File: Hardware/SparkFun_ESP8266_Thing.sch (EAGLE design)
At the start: 72 parts, among them J1 DNP, Q1 2.5A/30V, U1 ESP8266, U2 MCP73831, U3 AT25SF041-SOIC8, U4 AP2112K-3.3V, U5 DNP, U6 DNP, U7 DNP, Y1 26MHz

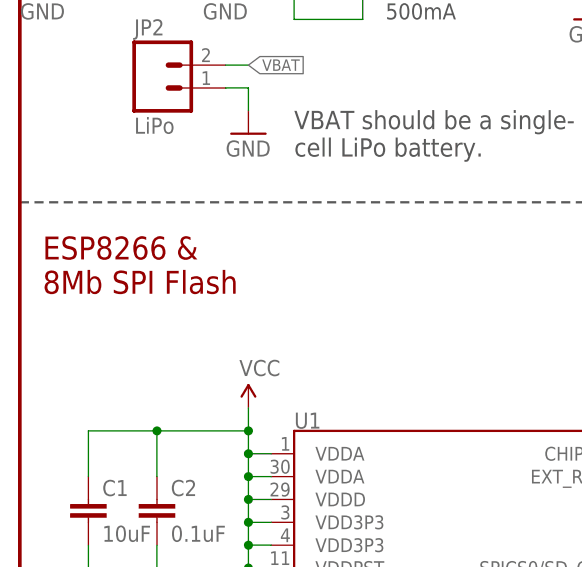
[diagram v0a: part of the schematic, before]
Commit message: Fixing flash size information in schematic.
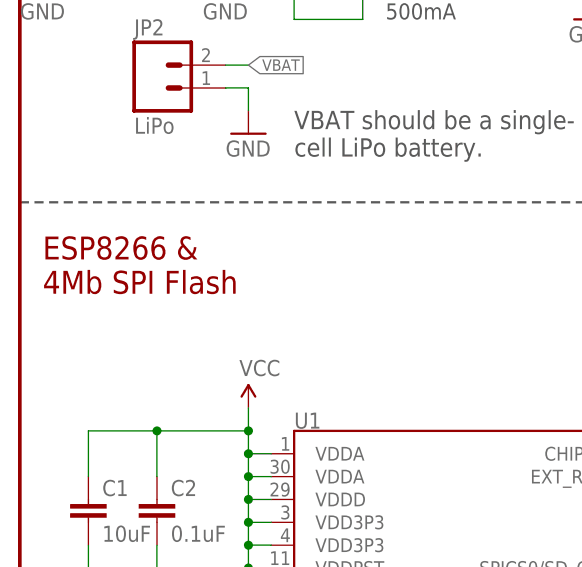
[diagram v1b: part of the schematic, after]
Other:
- note added: "ESP8266 & 4Mb SPI Flash"
- note removed: "ESP8266 & 8Mb SPI Flash"
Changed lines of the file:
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@@
 <layer number="254" name="cooling" color="7" fill="1" visible="yes" active="yes"/>
 </layers>
-<schematic xreflabel="%F%N/%S.%C%R" xrefpart="/%S.%C%R">
+<schematic xreflabel="%F%N/%S" xrefpart="/%S.%C%R">
 <attributes>
 </attributes>
@@
 LiPo Charger</text>
 <text x="2.54" y="116.84" size="2.54" layer="94">ESP8266 &amp;
-8Mb SPI Flash</text>
+4Mb SPI Flash</text>
 <text x="149.86" y="104.14" size="2.54" layer="94">Headers</text>
 <wire x1="147.32" y1="63.5" x2="248.92" y2="63.5" width="0.254" layer="97" style="shortdash"/>

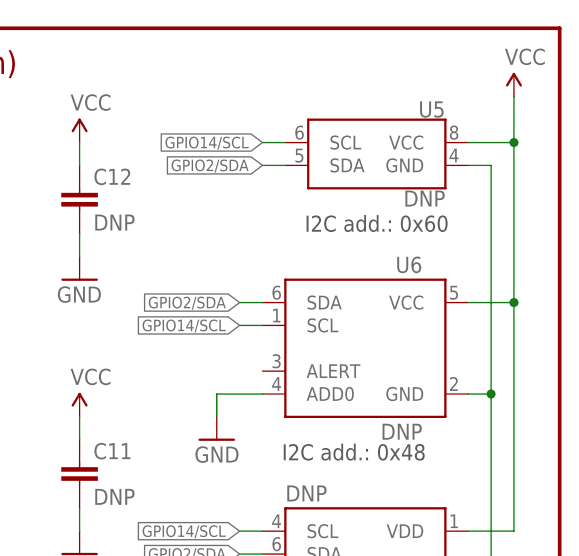
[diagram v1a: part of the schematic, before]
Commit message: Mapping new parts to equivalent devices in the SparkFun libraries.
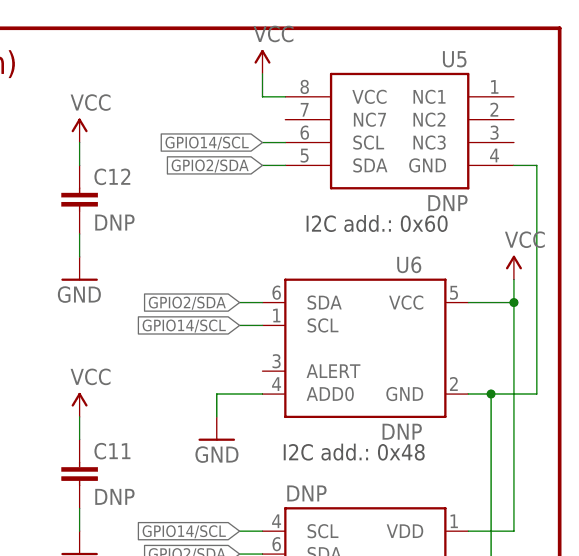
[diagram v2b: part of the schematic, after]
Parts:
- E1: device esp8266-development-board:ANTENNATRACE -> SparkFun-RF:ANTENNATRACE
- U1: device esp8266-development-board:ESP8266 -> SparkFun-RF:ESP8266
- U3: device esp8266-development-board:AT25SF041-SOIC8 -> SparkFun-DigitalIC:AT25SF041-SOIC8
- U5: device esp8266-development-board:ATECC108-MAHDA -> SparkFun-DigitalIC:ATECC108-MAHDA
- U7: device esp8266-development-board:TSL2561FN -> SparkFun-Sensors:TSL2561FN
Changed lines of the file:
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@@
 <layer number="56" name="wert" color="7" fill="1" visible="no" active="no"/>
 <layer number="57" name="tCAD" color="7" fill="1" visible="no" active="no"/>
+<layer number="59" name="tCarbon" color="7" fill="1" visible="no" active="no"/>
+<layer number="60" name="bCarbon" color="7" fill="1" visible="no" active="no"/>
 <layer number="90" name="Modules" color="5" fill="1" visible="yes" active="yes"/>
 <layer number="91" name="Nets" color="2" fill="1" visible="yes" active="yes"/>
@@
 <layer number="113" name="IDFDebug" color="7" fill="1" visible="yes" active="yes"/>
 <layer number="116" name="Patch_BOT" color="9" fill="4" visible="yes" active="yes"/>
+<layer number="118" name="Rect_Pads" color="7" fill="1" visible="yes" active="yes"/>
 <layer number="121" name="_tsilk" color="7" fill="1" visible="yes" active="yes"/>
 <layer number="122" name="_bsilk" color="7" fill="1" visible="yes" active="yes"/>
@@
 <layer number="127" name="_tValues" color="7" fill="1" visible="yes" active="yes"/>
 <layer number="128" name="_bValues" color="7" fill="1" visible="yes" active="yes"/>
+<layer number="129" name="Mask" color="7" fill="1" visible="yes" active="yes"/>
 <layer number="131" name="tAdjust" color="7" fill="1" visible="yes" active="yes"/>
 <layer number="132" name="bAdjust" color="7" fill="1" visible="yes" active="yes"/>
@@
 <layer number="251" name="SMDround" color="12" fill="11" visible="no" active="no"/>
 <layer number="254" name="cooling" color="7" fill="1" visible="yes" active="yes"/>
+<layer number="255" name="routoute" color="7" fill="1" visible="yes" active="yes"/>
 </layers>
 <schematic xreflabel="%F%N/%S" xrefpart="/%S.%C%R">
@@
 <parts>
 <part name="FRAME1" library="SparkFun-Aesthetics" deviceset="FRAME-LETTER" device=""/>
-<part name="U1" library="esp8266-development-board" deviceset="ESP8266" device=""/>
+<part name="U1" library="SparkFun-RF" deviceset="ESP8266" device=""/>
 <part name="SUPPLY1" library="SparkFun-Aesthetics" deviceset="VCC" device=""/>
 <part name="C1" library="SparkFun-Capacitors" deviceset="10UF-6.3V-20%(0603)" device="" value="10uF"/>
@@
 <part name="SUPPLY7" library="SparkFun-Aesthetics" deviceset="VCC" device=""/>
 <part name="GND20" library="SparkFun-Aesthetics" deviceset="GND" device=""/>
-<part name="U3" library="esp8266-development-board" deviceset="AT25SF041" device="-SOIC8"/>
-<part name="U5" library="esp8266-development-board" deviceset="ATECC108" device="-MAHDA" value="DNP"/>
+<part name="U3" library="SparkFun-DigitalIC" deviceset="AT25SF041" device="-SOIC8"/>
+<part name="U5" library="SparkFun-DigitalIC" deviceset="ATECC108" device="-MAHDA" value="DNP"/>
 <part name="SUPPLY13" library="SparkFun-Aesthetics" deviceset="VCC" device=""/>
 <part name="R13" library="SparkFun-Resistors" deviceset="2.2KOHM1/10W1%(0603)" device="" value="2.2k"/>
@@
 <part name="LOGO3" library="SparkFun-Aesthetics" deviceset="SFE_LOGO_FLAME" device=".1_INCH"/>
 <part name="LOGO4" library="SparkFun-Aesthetics" deviceset="OSHW-LOGO" device="S"/>
-<part name="E1" library="esp8266-development-board" deviceset="ANTENNA" device="TRACE" value="ANTENNATRACE"/>
+<part name="E1" library="SparkFun-RF" deviceset="ANTENNA" device="TRACE" value="ANTENNATRACE"/>
 <part name="GND18" library="SparkFun-Aesthetics" deviceset="GND" device=""/>
 <part name="C3" library="SparkFun-Capacitors" deviceset="10PF-50V-5%(0603)" device="" value="10pF"/>
@@
 <part name="SUPPLY12" library="SparkFun-Aesthetics" deviceset="VIN" device=""/>
 <part name="GND24" library="SparkFun-Aesthetics" deviceset="GND" device=""/>
-<part name="U7" library="esp8266-development-board" deviceset="TSL2561" device="FN" value="DNP"/>
+<part name="U7" library="SparkFun-Sensors" deviceset="TSL2561" device="FN" value="DNP"/>
 <part name="GND31" library="SparkFun-Aesthetics" deviceset="GND" device=""/>
 <part name="SUPPLY17" library="SparkFun-Aesthetics" deviceset="VCC" device=""/>
@@
 <part name="SJ1" library="SparkFun-Passives" deviceset="JUMPER-PAD-2-NC_BY_TRACE" device="" value=""/>
 <part name="R4" library="SparkFun-Resistors" deviceset="2.0KOHM1/10W5%(0603)" device="" value="2.0k"/>
+<part name="SUPPLY16" library="SparkFun-Aesthetics" deviceset="VCC" device=""/>
 </parts>
 <sheets>
@@
 <instance part="GND20" gate="1" x="139.7" y="7.62" rot="MR0"/>
 <instance part="U3" gate="G$1" x="109.22" y="17.78"/>
-<instance part="U5" gate="G$1" x="228.6" y="170.18" rot="MR0"/>
-<instance part="SUPPLY13" gate="G$1" x="243.84" y="177.8"/>
+<instance part="U5" gate="G$1" x="231.14" y="175.26" rot="MR0"/>
+<instance part="SUPPLY13" gate="G$1" x="243.84" y="157.48"/>
 <instance part="R13" gate="G$1" x="182.88" y="134.62" rot="R90"/>
 <instance part="R11" gate="G$1" x="167.64" y="134.62" rot="R90"/>
@@
 <attribute name="VALUE" x="68.326" y="154.686" size="1.778" layer="96" rot="MR270"/>
 </instance>
+<instance part="SUPPLY16" gate="G$1" x="215.9" y="180.34"/>
 </instances>
 <busses>
@@
 </segment>
 <segment>
+<pinref part="SUPPLY16" gate="G$1" pin="VCC"/>
+<pinref part="U5" gate="G$1" pin="VCC"/>
+<wire x1="218.44" y1="177.8" x2="215.9" y2="177.8" width="0.1524" layer="91"/>
+<wire x1="215.9" y1="177.8" x2="215.9" y2="180.34" width="0.1524" layer="91"/>
+</segment>
+<segment>
 <pinref part="U7" gate="G$1" pin="VDD"/>
 <wire x1="238.76" y1="129.54" x2="243.84" y2="129.54" width="0.1524" layer="91"/>
 <pinref part="U6" gate="G$1" pin="VCC"/>
 <wire x1="238.76" y1="154.94" x2="243.84" y2="154.94" width="0.1524" layer="91"/>
-<pinref part="U5" gate="G$1" pin="VCC"/>
-<wire x1="238.76" y1="172.72" x2="243.84" y2="172.72" width="0.1524" layer="91"/>
 <pinref part="SUPPLY13" gate="G$1" pin="VCC"/>
-<wire x1="243.84" y1="172.72" x2="243.84" y2="177.8" width="0.1524" layer="91"/>
-<wire x1="243.84" y1="154.94" x2="243.84" y2="172.72" width="0.1524" layer="91"/>
-<junction x="243.84" y="172.72"/>
+<wire x1="243.84" y1="154.94" x2="243.84" y2="157.48" width="0.1524" layer="91"/>
 <wire x1="243.84" y1="129.54" x2="243.84" y2="154.94" width="0.1524" layer="91"/>
 <junction x="243.84" y="154.94"/>
@@
 <segment>
 <pinref part="U5" gate="G$1" pin="GND"/>
-<wire x1="238.76" y1="170.18" x2="241.3" y2="170.18" width="0.1524" layer="91"/>
 <pinref part="U6" gate="G$1" pin="GND"/>
 <wire x1="238.76" y1="144.78" x2="241.3" y2="144.78" width="0.1524" layer="91"/>
@@
 <wire x1="241.3" y1="144.78" x2="241.3" y2="124.46" width="0.1524" layer="91"/>
 <junction x="241.3" y="124.46"/>
-<wire x1="241.3" y1="170.18" x2="241.3" y2="144.78" width="0.1524" layer="91"/>
+<wire x1="243.84" y1="170.18" x2="246.38" y2="170.18" width="0.1524" layer="91"/>
+<wire x1="246.38" y1="170.18" x2="246.38" y2="144.78" width="0.1524" layer="91"/>
+<wire x1="246.38" y1="144.78" x2="241.3" y2="144.78" width="0.1524" layer="91"/>
 <junction x="241.3" y="144.78"/>
 </segment>
